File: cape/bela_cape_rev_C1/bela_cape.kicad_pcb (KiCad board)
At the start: 4 copper layers, 71.8 x 54.6 mm, 143 parts, among them IC1 TLV320AIC3104, IC2 MIC5317, IC3 ES9080Q, IC4 LM4876, IC5 LM4876, IC6 TSV524xIQ4T, IC7 TSV524xIQ4T, IC8 ADS8168, J1 Conn_01x02, J10 Conn_01x04, J11 Conn_01x02, J12 Conn_01x03, J13 Conn_01x03, J14 Conn_01x03, J15 Conn_01x03, J2 Conn_01x04, J3 Conn_01x03, J4 Conn_01x03, J5 Conn_01x02, J6 Conn_01x02, J7 Conn_01x10, J8 Conn_01x10, J9 Conn_01x04, P1 BeagleBone_Black_Header, U1 TL974, U2 TL974

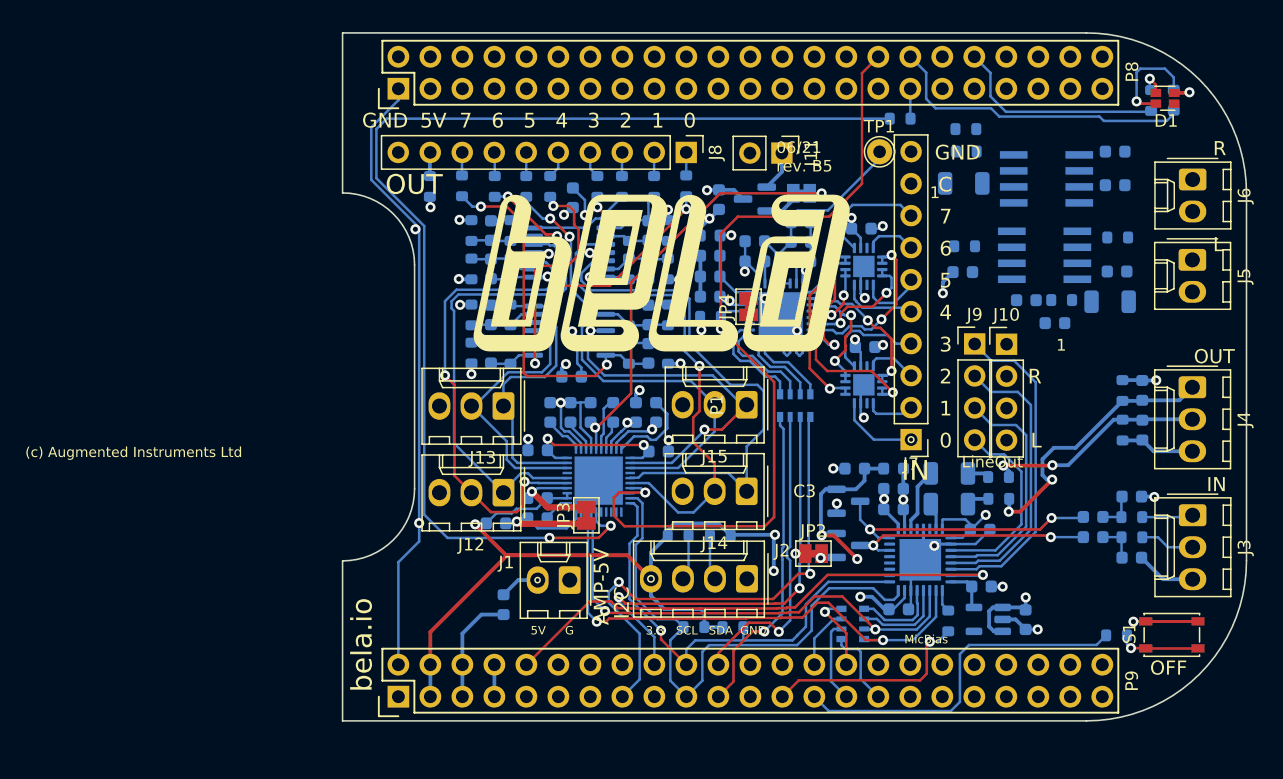
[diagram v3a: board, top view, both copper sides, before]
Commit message: First complete routing of C1 cape
(cherry picked from commit 8c5092941a0b3ec42f55098733fd0108b2086674)
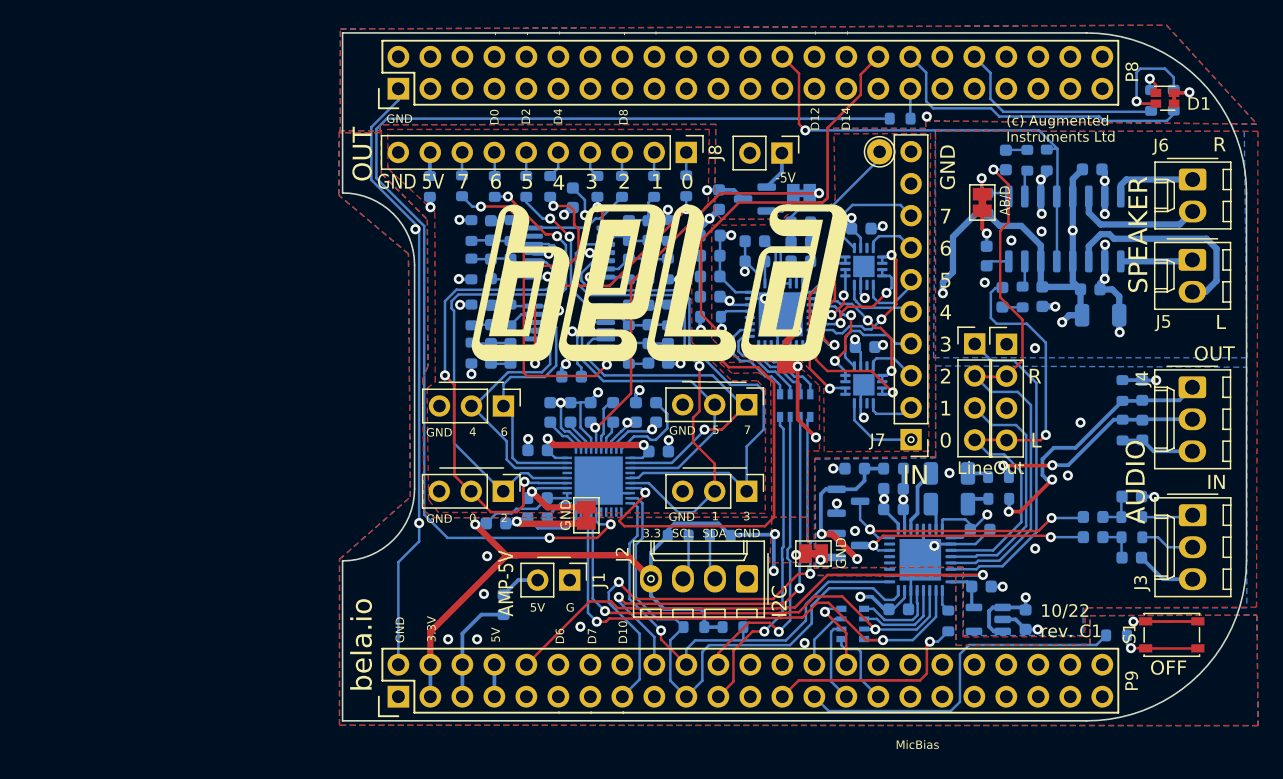
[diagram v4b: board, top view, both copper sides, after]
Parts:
- removed C21: 0.1uF, Capacitor_SMD:C_0603_1608Metric
- removed IC5: LM4876, bela_cape:SO8
- removed R10: 43k, Resistor_SMD:R_0603_1608Metric
- added JP5: SolderJumper_2_Bridged, Jumper:SolderJumper-2_P1.3mm_Bridged_Pad1.0x1.5mm, F.Cu at (163.4, 91.2)
- C14: value 0.1uF -> 1uF
- C17: value 47uF -> 0.1uF; footprint Capacitor_SMD:C_1206_3216Metric -> Capacitor_SMD:C_0603_1608Metric
- IC4: value LM4876 -> PAM8406; footprint bela_cape:SO8 -> Package_SO:SO-16_3.9x9.9mm_P1.27mm
- J1: footprint Connector_Molex:Molex_KK-254_AE-6410-02A_1x02_P2.54mm_Vertical -> Connector_PinHeader_2.54mm:PinHeader_1x02_P2.54mm_Vertical
- J12, J13, J14, J15: footprint Connector_Molex:Molex_KK-254_AE-6410-03A_1x03_P2.54mm_Vertical -> Connector_PinHeader_2.54mm:PinHeader_1x03_P2.54mm_Vertical
- JP4: footprint Jumper:SolderJumper-2_P1.3mm_Bridged_Pad1.0x1.5mm -> Bela:SolderJumper2_with_mask
- R6: value 22k -> 100k
- R9: value 43k -> 100k
- moved C16 15.1 mm to (172.8, 100.2), turned to 0 degrees
- moved C11 13.5 mm to (165.3, 87.8), turned to -90 degrees
- moved C14 13.1 mm to (163.8, 95.5), turned to 90 degrees
- moved R9 9.46 mm to (168.5, 87.8), turned to -90 degrees
- moved C20 6.62 mm to (168.2, 98.7), turned to 90 degrees
- moved R6 6.15 mm to (163.8, 91.3), turned to 90 degrees
- moved R7 4.89 mm to (167.0, 87.9), turned to 90 degrees
- moved JP4 4.38 mm to (146.4, 103.6)
- moved R8 3.11 mm to (166.6, 98.7), turned to -90 degrees
- moved IC4 2.63 mm to (169.9, 93.3), turned to 90 degrees
- moved C15 2.21 mm to (172.1, 88.6)
- moved C12 1.91 mm to (165.0, 98.8), turned to 90 degrees
- moved C17 1.85 mm to (172.0, 98.1)
- moved G1 0.79 mm to (137.2, 97.7)
- moved J12 0.11 mm to (125.4, 114.2), turned to -90 degrees
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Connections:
- C14 pad 1: GND -> Net-(C14-Pad1)
- C14 pad 2: Net-(C14-Pad2) -> GNDA
- C15 pad 1: GND -> GNDA
- C15 pad 2: Net-(C15-Pad2) -> +5V_AMP
- C16 pad 2: GND -> GNDA
- C17 pad 1: +5V_AMP -> GNDA
- C17 pad 2: GND -> +5V_AMP
- C20 pad 1: GND -> GNDA
- IC4 pad 1: AMP_SH/ -> /Audio Power Amp/AMP_OUTL+
- IC4 pad 2: Net-(C14-Pad2) -> GNDA
- IC4 pad 3: Net-(C14-Pad2) -> /Audio Power Amp/AMP_OUTL-
- IC4 pad 4: Net-(IC4-Pad4) -> +5V_AMP
- IC4 pad 5: /Audio Power Amp/AMP_OUTR- -> AMP_SH/
- IC4 pad 7: GND -> Net-(IC4-Pad7)
- IC4 pad 8: /Audio Power Amp/AMP_OUTR+ -> Net-(C14-Pad1)
- IC8 pad 8: unconnected-(IC8-Pad8) -> GNDA
- R6 pad 1: AMP_SH/ -> +5V_AMP
- R6 pad 2: GND -> Net-(IC4-Pad9)
- R7 pad 1: Net-(IC4-Pad4) -> Net-(IC4-Pad10)
- R8 pad 1: Net-(IC5-Pad4) -> Net-(IC4-Pad7)
- R9 pad 1: /Audio Power Amp/AMP_OUTR- -> AMP_SH/
- R9 pad 2: Net-(IC4-Pad4) -> GNDA
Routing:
- net +5V_AMP: track 55.0 -> 101.1 mm, vias 1 -> 4
- net AMP_SH/: track 0.00 -> 37.1 mm, vias 0 -> 1
- net GNDA: track 109.1 -> 132.3 mm, vias 31 -> 50
- net /Audio Power Amp/AMP_INR: track 0.00 -> 19.4 mm, vias 0 -> 1
- net /Audio Power Amp/AMP_INL: track 0.00 -> 18.9 mm, vias 0 -> 1
- net /Audio Power Amp/AMP_OUTL-: track 0.00 -> 17.1 mm
- net GND: track 96.1 -> 108.1 mm, vias 7 -> 16
- net /Audio Power Amp/AMP_OUTR-: track 0.00 -> 10.3 mm
- net /Audio Power Amp/AMP_OUTR+: track 0.00 -> 6.79 mm
- net /Audio Power Amp/AMP_OUTL+: track 0.00 -> 5.73 mm
- net Net-(IC4-Pad9): track 0.00 -> 4.45 mm, vias 0 -> 1
- net +5V: track 113.4 -> 110.0 mm
- net Net-(IC4-Pad10): track 0.00 -> 2.13 mm
- net Net-(IC4-Pad7): track 0.00 -> 2.07 mm
- net Net-(C14-Pad1): track 0.00 -> 1.90 mm
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- added copper zone on B.Cu, net +5V_AMP
- added copper zone on B.Cu, net GND
- added copper zone on F.Cu, net GND
- added copper zone on B.Cu, net GNDA
- added copper zone on F.Cu, net GNDA
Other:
- board text added: "-"
- board text added: "-5V"
- board text added: "10/22 rev. C1"
- board text added: "3.3V"
- board text added: "AB/D"
- board text added: "AUDIO"
- board text added: "D0"
- board text added: "D10"
- board text added: "D12"
- board text added: "D14"
- board text added: "D2"
- board text added: "D4"
- board text added: "D6"
- board text added: "D7"
- board text added: "D8"
- board text added: "SPEAKER"
- board text removed: "06/21 rev. B5"
- board text removed: "C"

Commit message: C1 cape: clean up bottom silkscreen
(cherry picked from commit 7c02b20f8f7a862246e5856b6fa8015b8ad6464b)
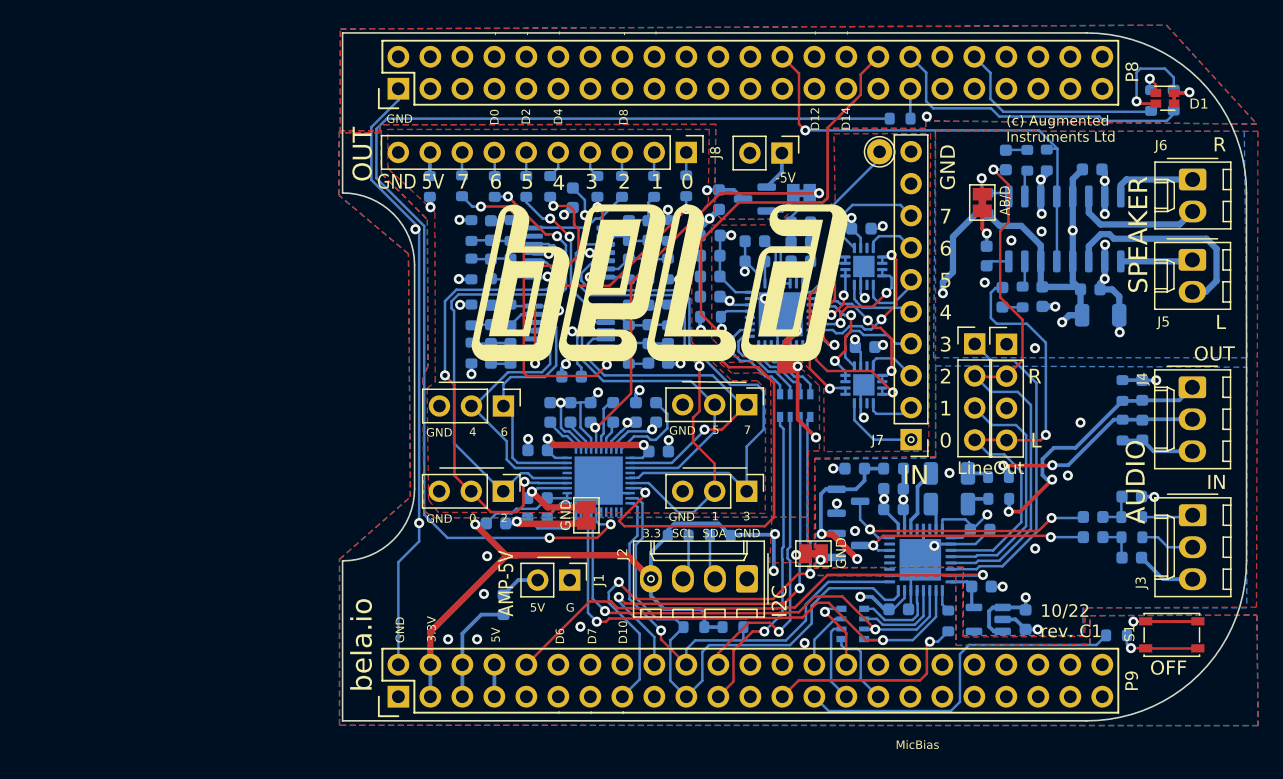
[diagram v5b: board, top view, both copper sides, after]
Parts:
- renumbered IC8 to IC5, U1 to IC8, U2 to IC9
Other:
- board text added: "-V"
- board text removed: "Vref"

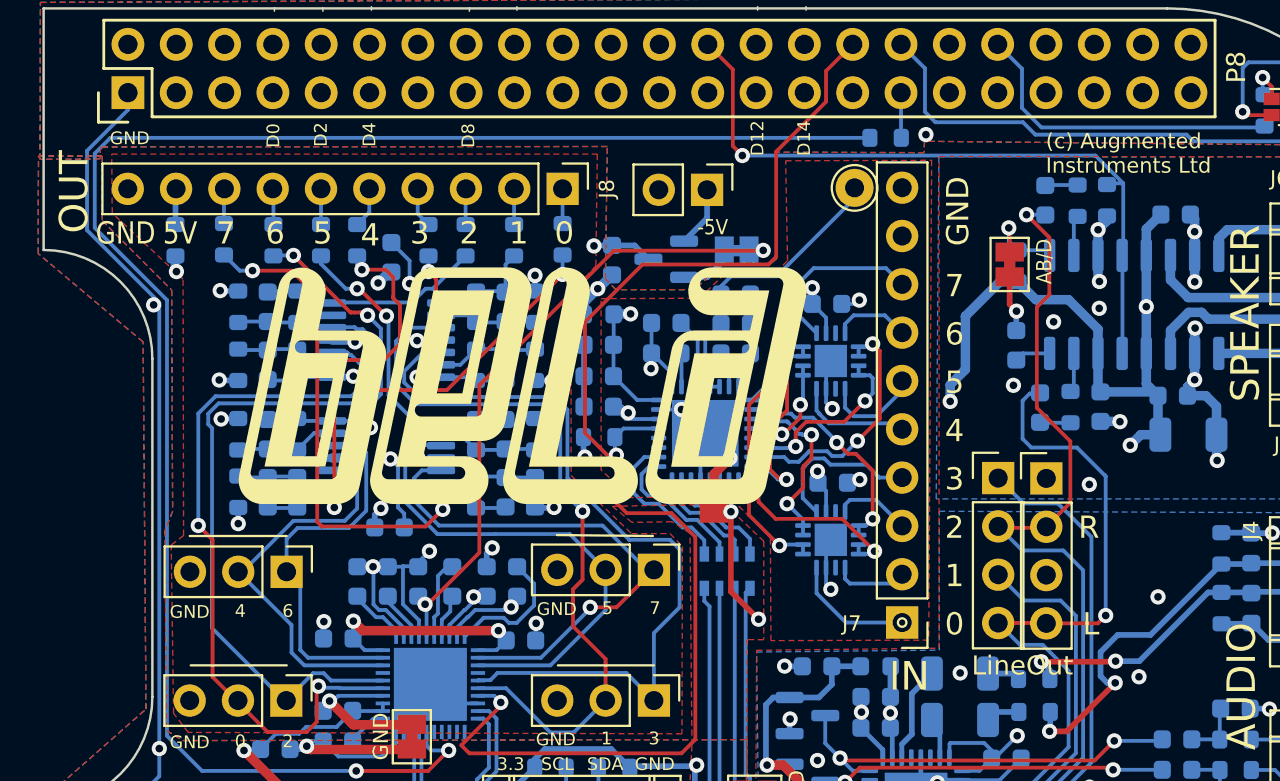
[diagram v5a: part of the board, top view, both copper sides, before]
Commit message: Further C1 cape updates
(cherry picked from commit 4c76e949636c5b1483c5ffba2ecc0f217292ab87)
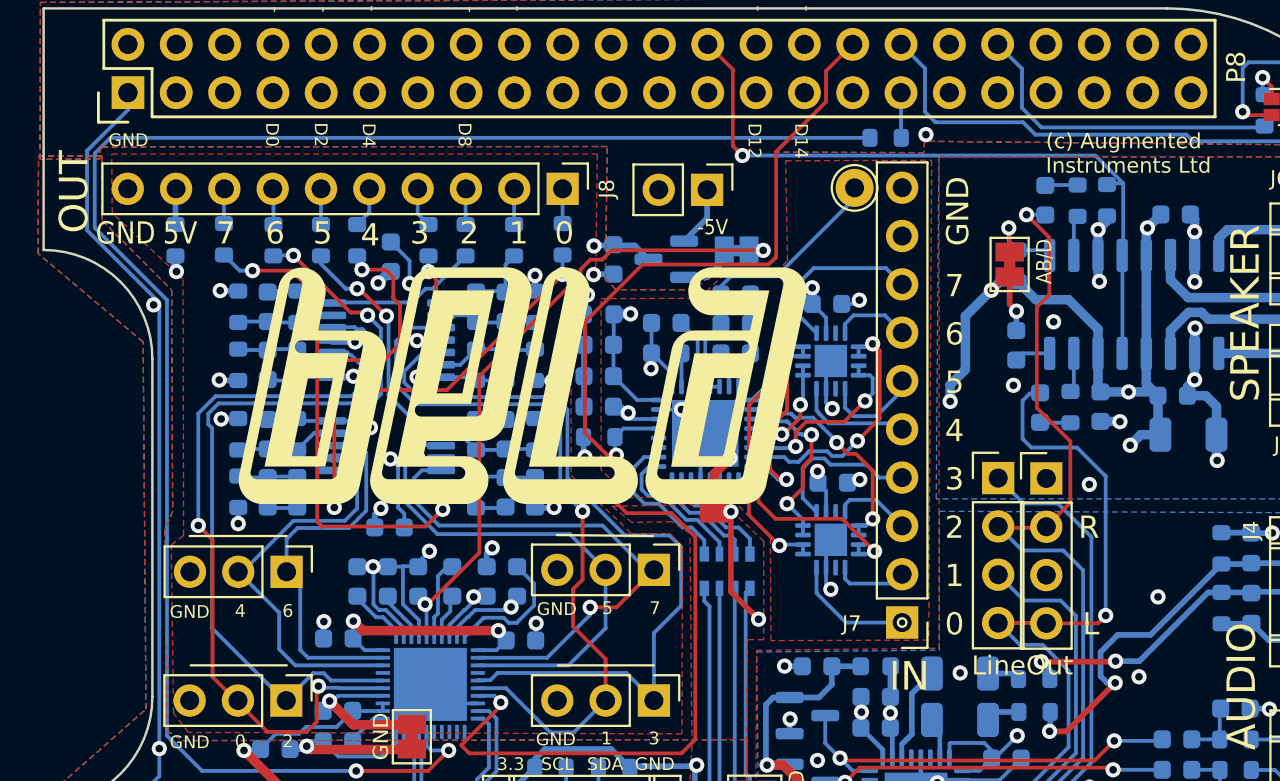
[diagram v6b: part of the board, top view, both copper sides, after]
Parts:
- R9: value 100k -> 4.7k
- moved C49 11.7 mm to (142.6, 91.0)
- moved C50 11.6 mm to (130.9, 90.8)
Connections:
- net Net-(C49-Pad1) renamed /Analog Output/DAC_OPAMP_V-
- C49 pad 2: +5V -> GNDA
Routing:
- net +5V: track 110.0 -> 91.8 mm
- net +5V_AMP: track 101.1 -> 98.6 mm, vias 4 -> 5
- net GNDA: track 132.3 -> 134.1 mm, vias 50 -> 51
- net /Analog Output/DAC5: track 26.7 -> 27.3 mm

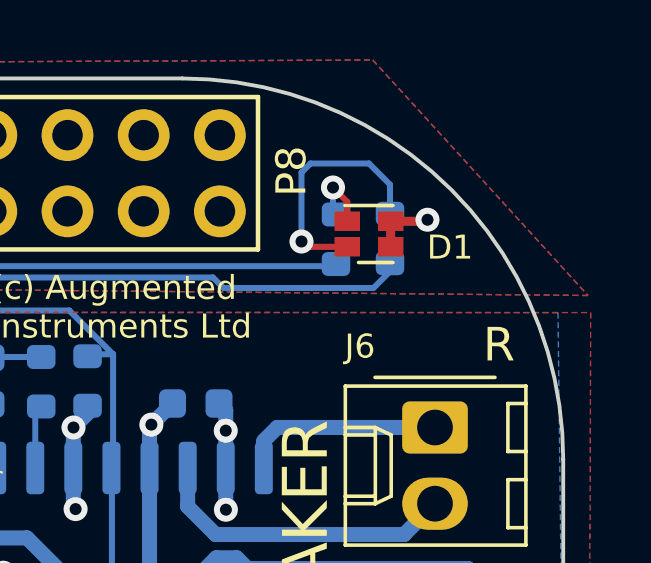
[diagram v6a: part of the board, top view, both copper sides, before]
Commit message: Bela cape C1: renumber components
(cherry picked from commit 6ebfe9c44bb7559ffb4c9dbd092e49803523e6a1)
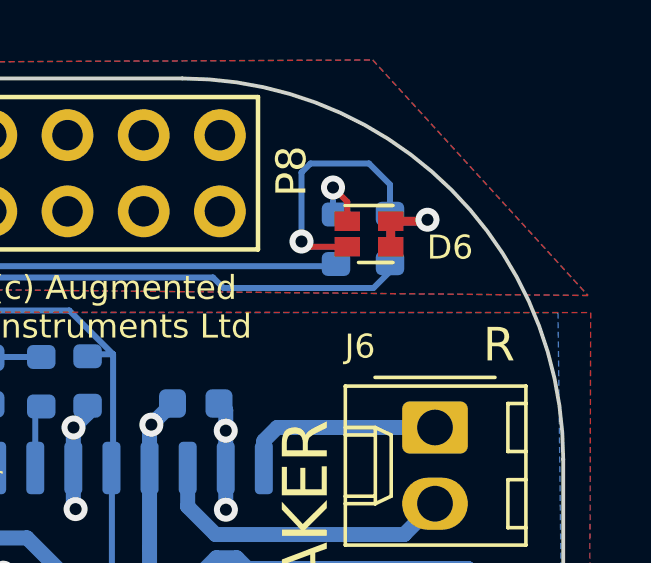
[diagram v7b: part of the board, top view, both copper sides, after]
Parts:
- renumbered C16 to C1, C9 to C10, C10 to C11, C13 to C12, C18 to C13, C1 to C14, C3 to C15, C52 to C16, C4 to C17, C5 to C18, C6 to C19, C20 to C2, C2 to C20, C31 to C21, C36 to C22, C19 to C23, C35 to C24, C41 to C25, C33 to C26, C40 to C27, C37 to C28, C48 to C29, C15 to C3, C32 to C30, C38 to C31, C42 to C32, C43 to C33, C47 to C34, C34 to C35, C39 to C36, C45 to C37, C46 to C38, C49 to C39, C17 to C4, C50 to C40, C51 to C41, C44 to C42, C53 to C43, C22 to C44, C23 to C45, C24 to C46, C25 to C47, C28 to C48, C27 to C49, C12 to C5, C29 to C50, C30 to C51, C26 to C52, C14 to C6, C11 to C7, C7 to C8, C8 to C9, D7 to D1, D8 to D2, D5 to D3, D6 to D4, D2 to D5, D1 to D6, FB3 to FB2, FB2 to FB3, IC4 to IC1, IC1 to IC2, IC2 to IC3, IC8 to IC4, IC9 to IC5, IC3 to IC6, IC6 to IC7, IC7 to IC8, IC5 to IC9, JP5 to JP1, JP1 to JP4, JP4 to JP5, R8 to R1, R23 to R10, R20 to R11, R25 to R12, R29 to R13, R33 to R14, R22 to R15, R27 to R16, R31 to R17, R36 to R18, R21 to R19, R7 to R2, R26 to R20, R30 to R21, R34 to R22, R24 to R23, R28 to R24, R32 to R25, R35 to R26, R39 to R27, R40 to R28, R41 to R29, R9 to R3, R42 to R30, R43 to R31, R44 to R32, R45 to R33, R46 to R34, R11 to R35, R18 to R36, R14 to R37, R15 to R38, R37 to R39, R6 to R4, R12 to R40, R13 to R41, R16 to R42, R17 to R43, R38 to R44, R19 to R45, R1 to R5, R2 to R6, R3 to R7, R4 to R8, R5 to R9, RN5 to RN1
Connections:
- C39 pad 2: GNDA -> unconnected-(C39-Pad2)
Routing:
- net GNDA: track 134.1 -> 129.4 mm, vias 51 -> 49
- net +5V_AMP: track 98.6 -> 101.6 mm, vias 5 -> 6
- net unconnected-(C39-Pad2): track 0.00 -> 1.72 mm, vias 0 -> 1
